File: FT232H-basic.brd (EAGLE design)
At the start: 45.7 x 20.3 mm, 29 parts, among them IC1 FT232H

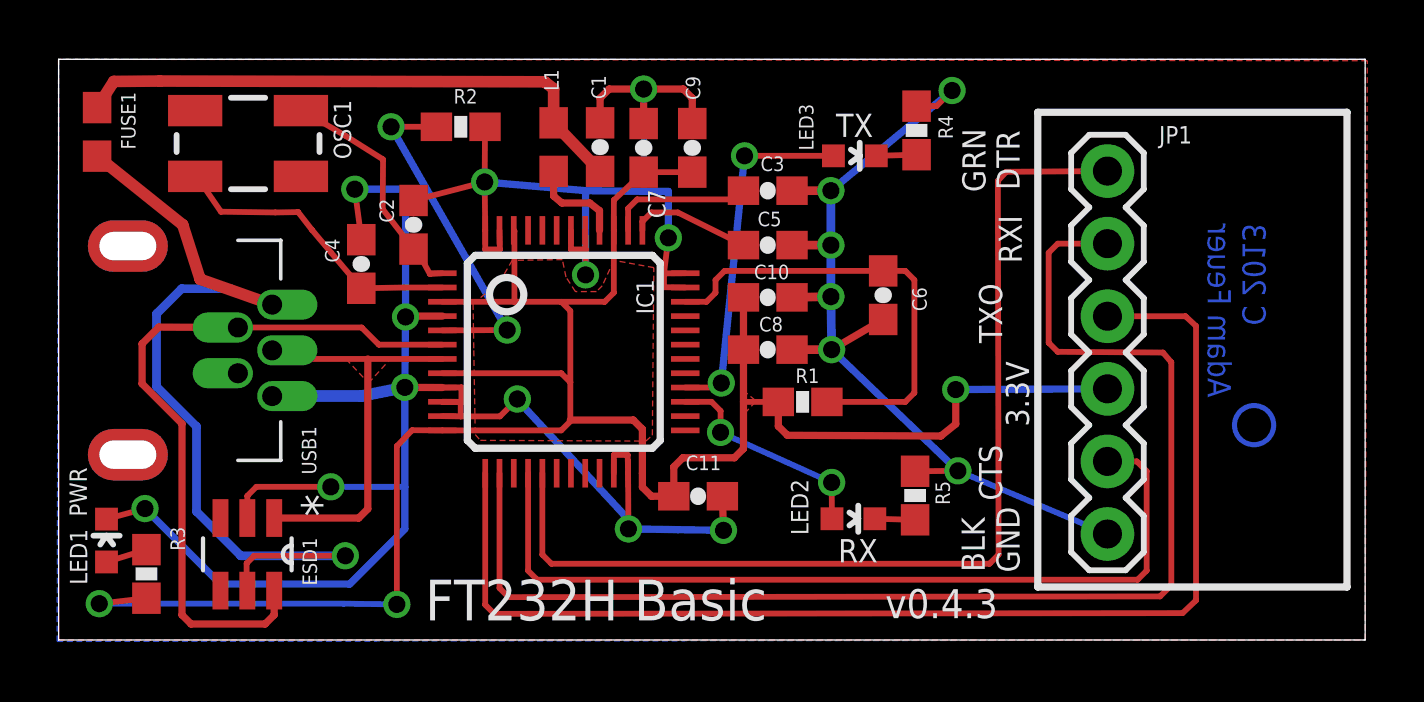
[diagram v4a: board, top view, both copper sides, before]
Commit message: fixed TX/RX led bug - TX/RX signals are active low, so need to be connected to power via 47O ohm resistor, as per UM232H datasheet
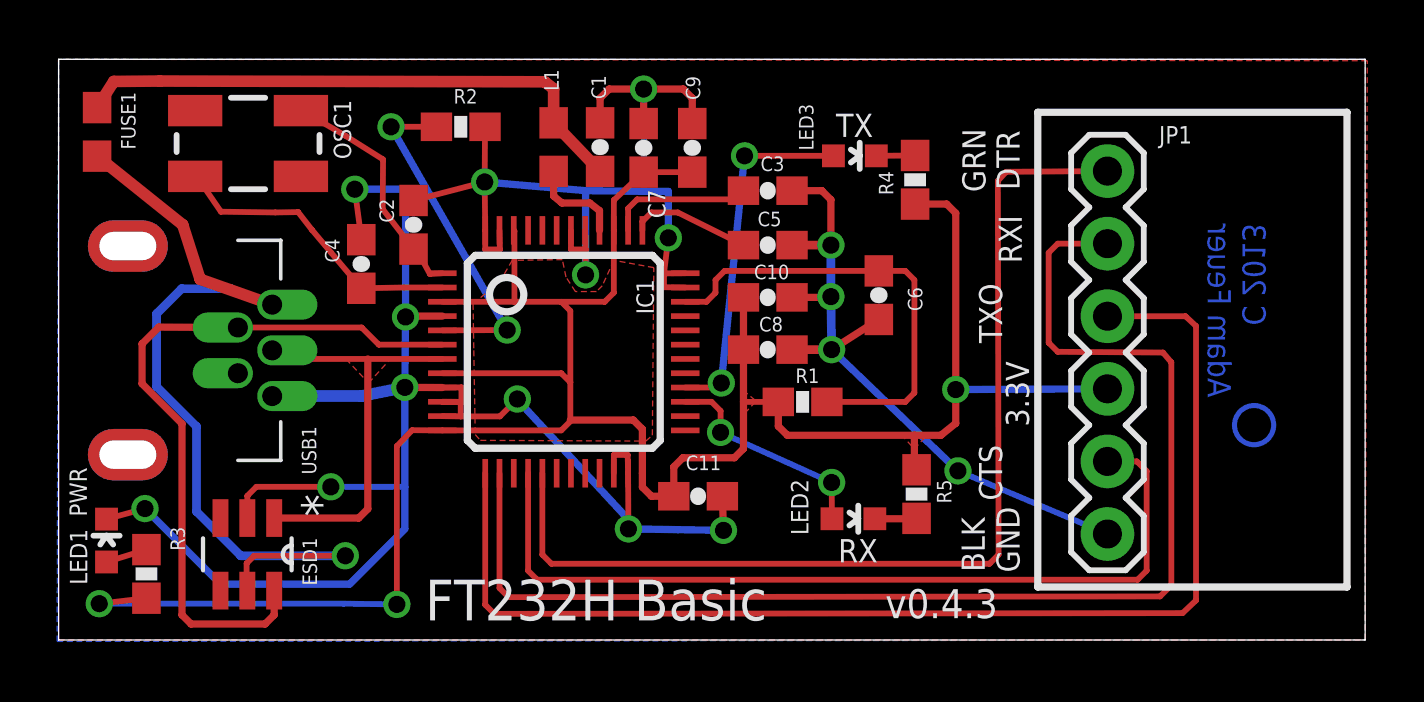
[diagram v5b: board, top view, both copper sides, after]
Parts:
- R4, R5: value 1k -> 470
- moved R4 1.73 mm to (36.3, 19.9), turned to 90 degrees
- moved C6 0.15 mm to (35.1, 15.9)
- moved R5 0.07 mm to (36.4, 8.92)
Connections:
- net GND: no longer R4.1, R5.1
- net POWER: now also R4.1, R5.1
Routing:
- net POWER: track 78.0 -> 86.9 mm
- net GND: track 130.1 -> 121.4 mm, vias 18 -> 16
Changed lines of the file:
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@@
 <attribute name="VALUE" x="21.4376" y="22.9108" size="0.4064" layer="27" font="vector" rot="R180"/>
 </element>
-<element name="C6" library="SparkFun-Capacitors" package="0603-CAP" value="10nF" x="35.2044" y="15.875" smashed="yes" rot="R270">
-<attribute name="PROD_ID" value="CAP-08604" x="-7.9756" y="0.635" size="1.778" layer="27" rot="R270" display="off"/>
-<attribute name="NAME" x="36.2204" y="16.1544" size="0.508" layer="25" font="vector" ratio="10" rot="R270"/>
-<attribute name="VALUE" x="34.0614" y="16.891" size="0.4064" layer="27" font="vector" rot="R270"/>
+<element name="C6" library="SparkFun-Capacitors" package="0603-CAP" value="10nF" x="35.052" y="15.875" smashed="yes" rot="R270">
+<attribute name="PROD_ID" value="CAP-08604" x="-8.128" y="0.635" size="1.778" layer="27" rot="R270" display="off"/>
+<attribute name="NAME" x="36.068" y="16.1544" size="0.508" layer="25" font="vector" ratio="10" rot="R270"/>
+<attribute name="VALUE" x="33.909" y="16.891" size="0.4064" layer="27" font="vector" rot="R270"/>
 </element>
 <element name="R1" library="SparkFun-Resistors" package="0603-RES" value="10K" x="32.385" y="12.1412" smashed="yes" rot="R180">
@@
 <attribute name="VALUE" x="33.1978" y="19.6723" size="0.4064" layer="27"/>
 </element>
-<element name="R4" library="SparkFun-Resistors" package="0603-RES" value="1k" x="36.3728" y="21.6408" smashed="yes" rot="R270">
-<attribute name="PROD_ID" value="RES-07856" x="-6.8072" y="-27.8892" size="1.778" layer="27" rot="R270" display="off"/>
-<attribute name="NAME" x="37.1348" y="22.1742" size="0.508" layer="25" font="vector" ratio="10" rot="R270"/>
-<attribute name="VALUE" x="35.2298" y="22.6568" size="0.4064" layer="27" font="vector" rot="R270"/>
-</element>
-<element name="R5" library="SparkFun-Resistors" package="0603-RES" value="1k" x="36.322" y="8.8646" smashed="yes" rot="R270">
-<attribute name="PROD_ID" value="RES-07856" x="-10.668" y="-6.3754" size="1.778" layer="27" rot="R270" display="off"/>
-<attribute name="NAME" x="37.0332" y="9.3726" size="0.508" layer="25" font="vector" ratio="10" rot="R270"/>
-<attribute name="VALUE" x="35.179" y="9.8806" size="0.4064" layer="27" font="vector" rot="R270"/>
+<element name="R4" library="SparkFun-Resistors" package="0603-RES" value="470" x="36.322" y="19.9136" smashed="yes" rot="R90">
+<attribute name="PROD_ID" value="RES-07856" x="79.502" y="69.4436" size="1.778" layer="27" rot="R90" display="off"/>
+<attribute name="NAME" x="35.56" y="19.3802" size="0.508" layer="25" font="vector" ratio="10" rot="R90"/>
+<attribute name="VALUE" x="37.465" y="18.8976" size="0.4064" layer="27" font="vector" rot="R90"/>
+</element>
+<element name="R5" library="SparkFun-Resistors" package="0603-RES" value="470" x="36.3728" y="8.9154" smashed="yes" rot="R270">
+<attribute name="PROD_ID" value="RES-07856" x="-10.6172" y="-6.3246" size="1.778" layer="27" rot="R270" display="off"/>
+<attribute name="NAME" x="37.084" y="9.4234" size="0.508" layer="25" font="vector" ratio="10" rot="R270"/>
+<attribute name="VALUE" x="35.2298" y="9.9314" size="0.4064" layer="27" font="vector" rot="R270"/>
 </element>
 <element name="LED1" library="SparkFun-LED" package="LED-0603" value="GREEN" x="8.0264" y="7.2898" smashed="yes">
@@
 <contactref element="C11" pad="2"/>
 <contactref element="USB1" pad="GND"/>
-<contactref element="R4" pad="1"/>
-<contactref element="R5" pad="1"/>
 <contactref element="LED1" pad="C"/>
 <polygon width="0.254" layer="16">
@@
 <wire x1="43.053" y1="7.5184" x2="37.8206" y2="9.7282" width="0.2032" layer="16"/>
 <via x="37.8206" y="9.7282" extent="1-16" drill="0.6"/>
-<wire x1="37.8206" y1="9.7282" x2="36.322" y2="9.7146" width="0.2032" layer="1"/>
 <wire x1="25.7784" y1="9.6438" x2="25.781" y2="10.287" width="0.2032" layer="1"/>
 <wire x1="25.781" y1="10.287" x2="26.2636" y2="10.287" width="0.2032" layer="1"/>
@@
 <wire x1="21.7932" y1="17.4752" x2="21.2784" y2="17.4752" width="0.2032" layer="1"/>
 <wire x1="8.0264" y1="8.0398" x2="9.3726" y2="8.4074" width="0.2032" layer="1"/>
-<wire x1="32.0158" y1="19.5326" x2="33.3756" y2="19.5326" width="0.3048" layer="1"/>
-<via x="33.3756" y="19.5326" extent="1-16" drill="0.6"/>
 <wire x1="27.686" y1="19.5072" x2="26.8478" y2="19.5072" width="0.254" layer="16"/>
 <wire x1="26.8478" y1="19.5072" x2="24.7904" y2="19.5326" width="0.254" layer="16"/>
@@
 <wire x1="32.0158" y1="17.6276" x2="33.3756" y2="17.6276" width="0.3048" layer="1"/>
 <via x="33.3756" y="17.6276" extent="1-16" drill="0.6"/>
-<wire x1="33.3756" y1="17.6276" x2="33.3756" y2="19.5326" width="0.3048" layer="16"/>
-<wire x1="32.0158" y1="15.7988" x2="33.3756" y2="15.8242" width="0.3048" layer="1"/>
 <via x="33.3756" y="15.8242" extent="1-16" drill="0.6"/>
 <wire x1="33.3756" y1="15.8242" x2="33.3756" y2="17.6276" width="0.3048" layer="16"/>
@@
 <wire x1="29.6164" y1="7.6454" x2="28.0162" y2="7.6708" width="0.254" layer="16"/>
 <wire x1="37.8206" y1="9.7282" x2="33.401" y2="13.97" width="0.254" layer="16"/>
-<wire x1="35.2044" y1="15.025" x2="33.401" y2="13.97" width="0.254" layer="1"/>
+<wire x1="35.052" y1="15.025" x2="33.401" y2="13.97" width="0.254" layer="1"/>
 <via x="21.2598" y="19.8374" extent="1-16" drill="0.6"/>
 <wire x1="19.7784" y1="15.1438" x2="18.4912" y2="15.1438" width="0.254" layer="1"/>
@@
 <via x="18.4658" y="12.6492" extent="1-16" drill="0.6"/>
 <wire x1="18.4658" y1="12.6492" x2="18.4912" y2="15.113" width="0.254" layer="16"/>
-<wire x1="36.3728" y1="22.4908" x2="37.0704" y2="22.4908" width="0.2032" layer="1"/>
-<wire x1="37.0704" y1="22.4908" x2="37.6174" y2="23.0378" width="0.2032" layer="1"/>
-<via x="37.6174" y="23.0378" extent="1-16" drill="0.6"/>
-<wire x1="33.3756" y1="19.5326" x2="37.6174" y2="23.0378" width="0.254" layer="16"/>
 <wire x1="21.2716" y1="21.7678" x2="21.2598" y2="19.8374" width="0.2032" layer="1"/>
 <wire x1="16.9418" y1="17.8172" x2="16.9418" y2="17.868" width="0.2032" layer="1"/>
@@
 <wire x1="13.8238" y1="12.3446" x2="16.942" y2="12.3446" width="0.4064" layer="16"/>
 <wire x1="16.942" y1="12.3446" x2="18.4658" y2="12.6492" width="0.4064" layer="16"/>
+<wire x1="32.0158" y1="19.5326" x2="33.0581" y2="19.5326" width="0.254" layer="1"/>
+<wire x1="33.0581" y1="19.5326" x2="33.3756" y2="19.2151" width="0.254" layer="1"/>
+<wire x1="33.3756" y1="19.2151" x2="33.3756" y2="17.6276" width="0.254" layer="1"/>
+<wire x1="32.0158" y1="15.7988" x2="33.3502" y2="15.7988" width="0.254" layer="1"/>
+<wire x1="33.3502" y1="15.7988" x2="33.3756" y2="15.8242" width="0.254" layer="1"/>
 </signal>
 <signal name="OSC1">
@@
 <wire x1="29.337" y1="15.9613" x2="29.337" y2="16.4075" width="0.2032" layer="1"/>
 <wire x1="29.337" y1="16.4075" x2="29.6545" y2="16.725" width="0.2032" layer="1"/>
-<wire x1="29.6545" y1="16.725" x2="35.2044" y2="16.725" width="0.2032" layer="1"/>
-<wire x1="35.2044" y1="16.725" x2="35.9791" y2="16.725" width="0.2032" layer="1"/>
+<wire x1="29.6545" y1="16.725" x2="35.052" y2="16.725" width="0.2032" layer="1"/>
+<wire x1="35.052" y1="16.725" x2="35.9791" y2="16.725" width="0.2032" layer="1"/>
 <wire x1="35.9791" y1="16.725" x2="36.2966" y2="16.4075" width="0.2032" layer="1"/>
 <wire x1="36.2966" y1="16.4075" x2="36.2966" y2="12.4587" width="0.2032" layer="1"/>
@@
 <wire x1="31.535" y1="12.1412" x2="31.535" y2="11.2903" width="0.254" layer="1"/>
 <wire x1="31.535" y1="11.2903" x2="31.8525" y2="10.9728" width="0.254" layer="1"/>
-<wire x1="31.8525" y1="10.9728" x2="37.2237" y2="10.9474" width="0.254" layer="1"/>
-<wire x1="37.2237" y1="10.9474" x2="37.7444" y2="11.3665" width="0.254" layer="1"/>
+<wire x1="31.8525" y1="10.9728" x2="36.2966" y2="10.9728" width="0.254" layer="1"/>
+<wire x1="36.2966" y1="10.9728" x2="37.2237" y2="10.9728" width="0.254" layer="1"/>
+<wire x1="37.2237" y1="10.9728" x2="37.7444" y2="11.3919" width="0.254" layer="1"/>
 <polygon width="0" layer="1">
 <vertex x="30.3022" y="12.5476"/>
@@
 <vertex x="20.8534" y="15.5702"/>
 </polygon>
-<wire x1="37.7444" y1="11.3665" x2="37.7444" y2="12.573" width="0.254" layer="1"/>
+<wire x1="37.7444" y1="11.3919" x2="37.7444" y2="12.573" width="0.254" layer="1"/>
 <via x="37.7444" y="12.573" extent="1-16" drill="0.6"/>
 <wire x1="37.7444" y1="12.573" x2="43.053" y2="12.5984" width="0.254" layer="16"/>
+<contactref element="R4" pad="1"/>
+<wire x1="36.322" y1="19.0636" x2="37.4269" y2="19.0636" width="0.254" layer="1"/>
+<wire x1="37.4269" y1="19.0636" x2="37.7444" y2="18.7461" width="0.254" layer="1"/>
+<wire x1="37.7444" y1="18.7461" x2="37.7444" y2="12.573" width="0.254" layer="1"/>
+<contactref element="R5" pad="1"/>
+<wire x1="36.3728" y1="9.7654" x2="36.2966" y2="9.8416" width="0.254" layer="1"/>
+<wire x1="36.2966" y1="9.8416" x2="36.2966" y2="10.9728" width="0.254" layer="1"/>
+<polygon width="0" layer="1">
+<vertex x="35.8394" y="10.9982"/>
+<vertex x="36.2966" y="10.4902"/>
+<vertex x="36.7538" y="10.9982"/>
+</polygon>
 </signal>
 <signal name="TXO">
@@
 <contactref element="LED3" pad="C"/>
 <contactref element="R4" pad="2"/>
-<wire x1="34.9638" y1="20.7518" x2="36.3728" y2="20.7908" width="0.2032" layer="1"/>
+<wire x1="34.9638" y1="20.7518" x2="36.322" y2="20.7636" width="0.2032" layer="1"/>
 </signal>
 <signal name="N$11">
 <contactref element="LED2" pad="C"/>
 <contactref element="R5" pad="2"/>
-<wire x1="34.913" y1="8.0518" x2="36.322" y2="8.0146" width="0.2032" layer="1"/>
+<wire x1="34.913" y1="8.0518" x2="36.3592" y2="8.0518" width="0.254" layer="1"/>
+<wire x1="36.3592" y1="8.0518" x2="36.3728" y2="8.0654" width="0.254" layer="1"/>
 </signal>
 <signal name="VREGIN">

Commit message: fixed LED orientation - anode faces power
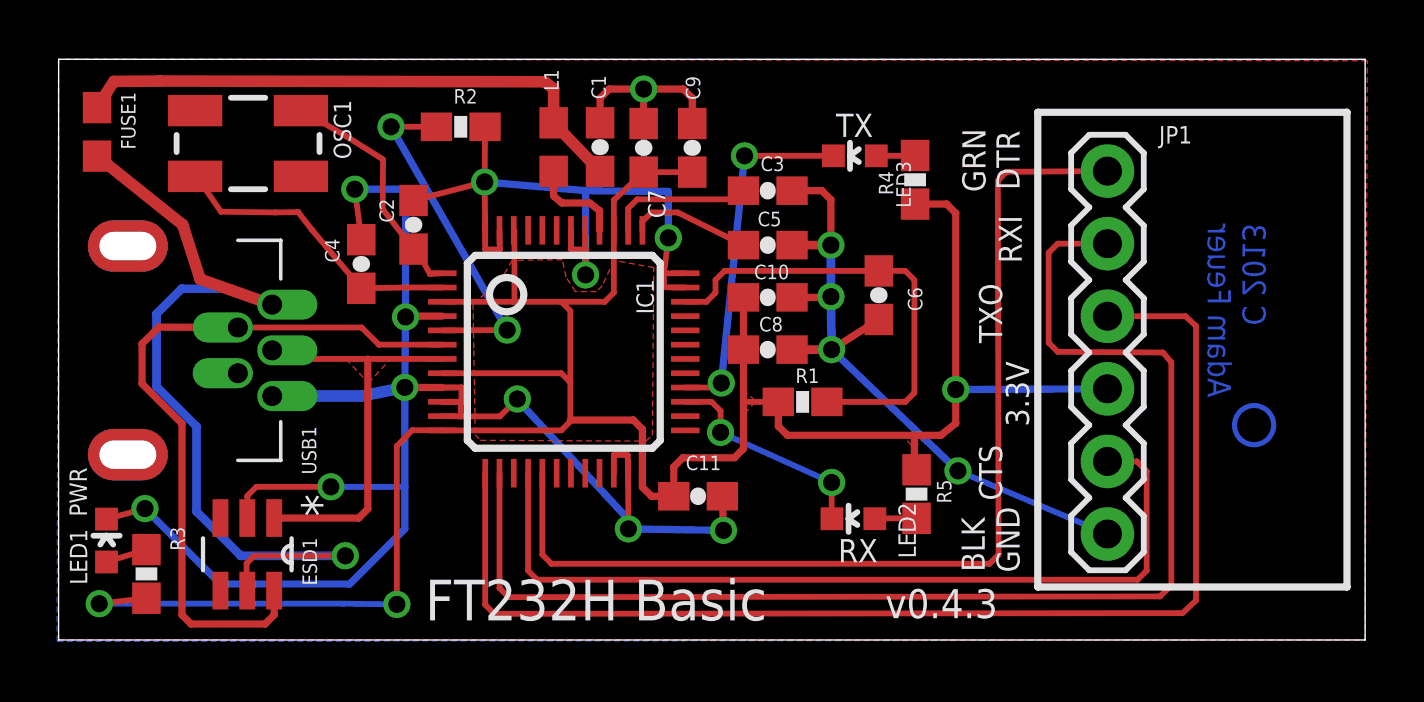
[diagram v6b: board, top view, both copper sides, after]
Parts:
- turned LED2 to 90 degrees
- turned LED3 to 90 degrees
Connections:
- removed net N$11: LED2.C, R5.2
- new net N$8: LED3.A, R4.2
- net N$10: now also LED2.A, R5.2; no longer LED3.C, R4.2
- net RXLED: now also LED2.C; no longer LED2.A
- net TXLED: now also LED3.C; no longer LED3.A
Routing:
- net N$11: track 1.47 -> 0.00 mm
- net N$8: track 0.00 -> 1.37 mm
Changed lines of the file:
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@@
 <attribute name="VALUE" x="7.5438" y="11.4046" size="0.4064" layer="27" font="vector" rot="R90"/>
 </element>
-<element name="LED2" library="SparkFun-LED" package="LED-0603" value="GREEN" x="34.163" y="8.0518" smashed="yes" rot="R270">
-<attribute name="PROD_ID" value="DIO-00821" x="-12.827" y="-10.9982" size="1.778" layer="27" rot="R270" display="off"/>
-<attribute name="NAME" x="31.9786" y="9.4361" size="0.6096" layer="25" font="vector" ratio="10" rot="R270"/>
-<attribute name="VALUE" x="33.147" y="6.9723" size="0.4064" layer="27"/>
-</element>
-<element name="LED3" library="SparkFun-LED" package="LED-0603" value="YELLOW" x="34.2138" y="20.7518" smashed="yes" rot="R270">
-<attribute name="PROD_ID" value="DIO-09003" x="-2.6162" y="-4.6482" size="1.778" layer="27" rot="R270" display="off"/>
-<attribute name="NAME" x="32.258" y="22.5679" size="0.508" layer="25" font="vector" ratio="10" rot="R270"/>
-<attribute name="VALUE" x="33.1978" y="19.6723" size="0.4064" layer="27"/>
+<element name="LED2" library="SparkFun-LED" package="LED-0603" value="GREEN" x="34.163" y="8.0518" smashed="yes" rot="R90">
+<attribute name="PROD_ID" value="DIO-00821" x="81.153" y="27.1018" size="1.778" layer="27" rot="R90" display="off"/>
+<attribute name="NAME" x="36.3474" y="6.6675" size="0.6096" layer="25" font="vector" ratio="10" rot="R90"/>
+<attribute name="VALUE" x="35.179" y="9.1313" size="0.4064" layer="27" rot="R180"/>
+</element>
+<element name="LED3" library="SparkFun-LED" package="LED-0603" value="YELLOW" x="34.2138" y="20.7518" smashed="yes" rot="R90">
+<attribute name="PROD_ID" value="DIO-09003" x="71.0438" y="46.1518" size="1.778" layer="27" rot="R90" display="off"/>
+<attribute name="NAME" x="36.1696" y="18.9357" size="0.508" layer="25" font="vector" ratio="10" rot="R90"/>
+<attribute name="VALUE" x="35.2298" y="21.8313" size="0.4064" layer="27" rot="R180"/>
 </element>
 <element name="R4" library="SparkFun-Resistors" package="0603-RES" value="470" x="36.322" y="19.9136" smashed="yes" rot="R90">
@@
 <wire x1="36.2966" y1="9.8416" x2="36.2966" y2="10.9728" width="0.254" layer="1"/>
 <polygon width="0" layer="1">
-<vertex x="35.8394" y="10.9982"/>
-<vertex x="36.2966" y="10.4902"/>
+<vertex x="35.814" y="11.0236"/>
+<vertex x="36.2966" y="10.5156"/>
 <vertex x="36.7538" y="10.9982"/>
 </polygon>
@@
 <signal name="RXLED">
 <contactref element="IC1" pad="27"/>
-<contactref element="LED2" pad="A"/>
 <wire x1="28.2784" y1="12.1438" x2="29.1973" y2="12.1438" width="0.2032" layer="1"/>
 <wire x1="29.1973" y1="12.1438" x2="29.5148" y2="11.8263" width="0.2032" layer="1"/>
@@
 <wire x1="29.5148" y1="11.0744" x2="33.401" y2="9.3218" width="0.2032" layer="16"/>
 <via x="33.401" y="9.3218" extent="1-16" drill="0.6"/>
-<wire x1="33.401" y1="9.3218" x2="33.413" y2="8.0518" width="0.2032" layer="1"/>
+<contactref element="LED2" pad="C"/>
+<wire x1="33.413" y1="8.0518" x2="33.401" y2="8.0518" width="0.2032" layer="1"/>
+<wire x1="33.401" y1="8.0518" x2="33.401" y2="9.3218" width="0.2032" layer="1"/>
 </signal>
 <signal name="TXLED">
 <contactref element="IC1" pad="28"/>
-<contactref element="LED3" pad="A"/>
 <wire x1="28.2784" y1="12.6438" x2="29.3824" y2="12.6438" width="0.2032" layer="1"/>
 <wire x1="29.3824" y1="12.6438" x2="29.5402" y2="12.8016" width="0.2032" layer="1"/>
 <via x="29.5402" y="12.8016" extent="1-16" drill="0.6"/>
 <via x="30.353" y="20.7518" extent="1-16" drill="0.6"/>
+<wire x1="29.5402" y1="12.8016" x2="30.353" y2="20.7518" width="0.254" layer="16"/>
+<contactref element="LED3" pad="C"/>
 <wire x1="30.353" y1="20.7518" x2="33.4638" y2="20.7518" width="0.2032" layer="1"/>
-<wire x1="29.5402" y1="12.8016" x2="30.353" y2="20.7518" width="0.254" layer="16"/>
-</signal>
-<signal name="N$10">
-<contactref element="LED3" pad="C"/>
-<contactref element="R4" pad="2"/>
-<wire x1="34.9638" y1="20.7518" x2="36.322" y2="20.7636" width="0.2032" layer="1"/>
-</signal>
-<signal name="N$11">
-<contactref element="LED2" pad="C"/>
-<contactref element="R5" pad="2"/>
-<wire x1="34.913" y1="8.0518" x2="36.3592" y2="8.0518" width="0.254" layer="1"/>
-<wire x1="36.3592" y1="8.0518" x2="36.3728" y2="8.0654" width="0.254" layer="1"/>
 </signal>
 <signal name="VREGIN">
@@
 <wire x1="8.2804" y1="23.3553" x2="7.6962" y2="22.44" width="0.4064" layer="1"/>
 </signal>
+<signal name="N$10">
+<contactref element="R5" pad="2"/>
+<contactref element="LED2" pad="A"/>
+<wire x1="36.3728" y1="8.0654" x2="34.913" y2="8.0654" width="0.2032" layer="1"/>
+<wire x1="34.913" y1="8.0654" x2="34.913" y2="8.0518" width="0.2032" layer="1"/>
+</signal>
+<signal name="N$8">
+<contactref element="LED3" pad="A"/>
+<contactref element="R4" pad="2"/>
+<wire x1="34.9638" y1="20.7518" x2="36.322" y2="20.7518" width="0.2032" layer="1"/>
+<wire x1="36.322" y1="20.7518" x2="36.322" y2="20.7636" width="0.2032" layer="1"/>
+</signal>
 </signals>
